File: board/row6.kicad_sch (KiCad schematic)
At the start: 0 parts

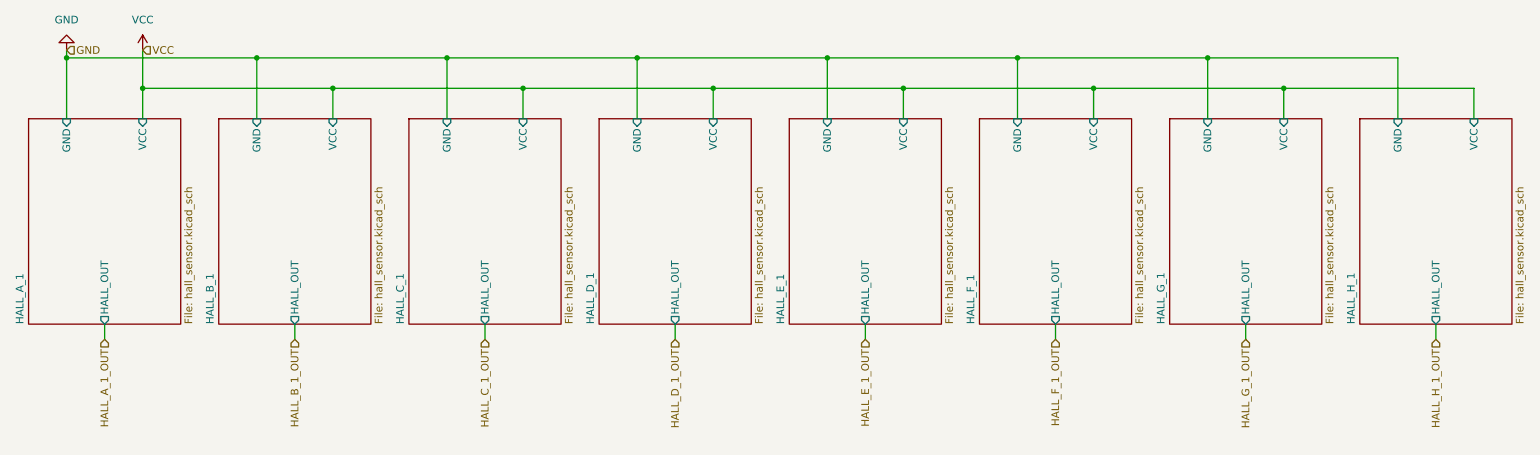
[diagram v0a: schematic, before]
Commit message: Connected all rows to MCPs
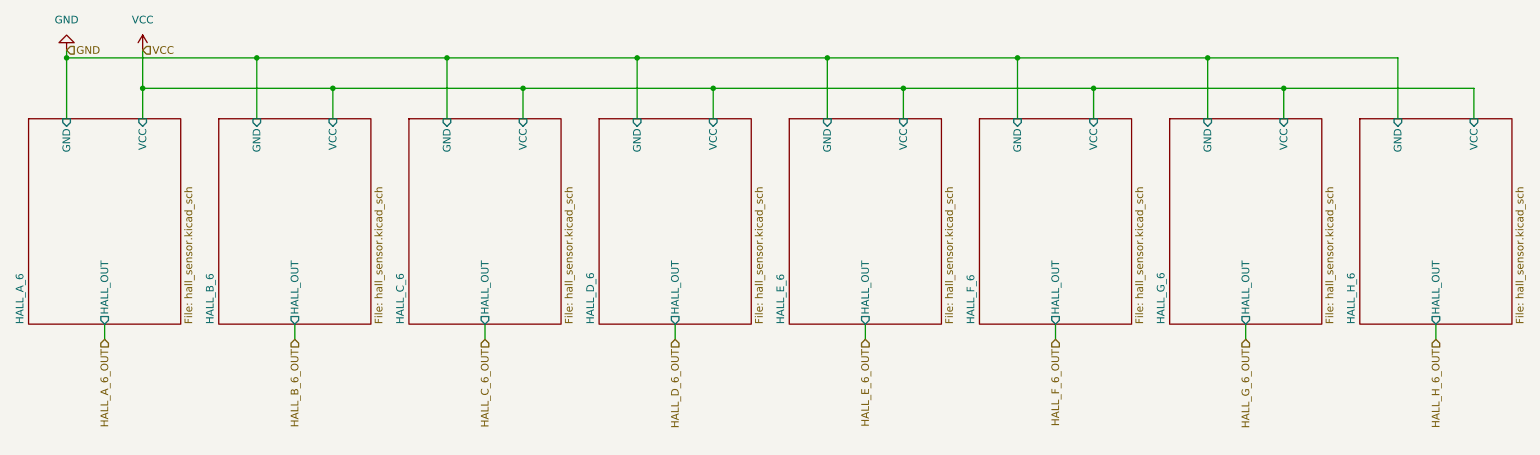
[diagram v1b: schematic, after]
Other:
- removed sheet HALL_A_1
- removed sheet HALL_B_1
- removed sheet HALL_C_1
- removed sheet HALL_D_1
- removed sheet HALL_E_1
- removed sheet HALL_F_1
- removed sheet HALL_G_1
- removed sheet HALL_H_1
- added sheet HALL_A_6 (hall_sensor.kicad_sch)
- added sheet HALL_B_6 (hall_sensor.kicad_sch)
- added sheet HALL_C_6 (hall_sensor.kicad_sch)
- added sheet HALL_D_6 (hall_sensor.kicad_sch)
- added sheet HALL_E_6 (hall_sensor.kicad_sch)
- added sheet HALL_F_6 (hall_sensor.kicad_sch)
- added sheet HALL_G_6 (hall_sensor.kicad_sch)
- added sheet HALL_H_6 (hall_sensor.kicad_sch)
